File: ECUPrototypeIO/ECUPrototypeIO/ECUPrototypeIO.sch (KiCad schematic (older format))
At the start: 49 parts, among them K1 Relay, K2 Relay, K3 Relay, K4 Relay, K5 Relay, K6 Relay, K7 Relay, K8 Relay, Q1 PN2222A, Q2 PN2222A, Q3 PN2222A, Q4 PN2222A, Q5 PN2222A, SW1 MomentarySwitch, SW2 MomentarySwitch, U1 LM358

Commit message: Sam's Edits (Early January)
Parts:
- removed C3: 470uF, symbol Device:CP1
- removed C4: 1000uF, symbol Device:CP1
- removed D1, D2, D3, D4, D5, D6, D7, D8: D, symbol Device:D
- removed K4, K7: Relay, Relay_THT:Relay_StandexMeder_DIP_LowProfile, symbol Relay:DIPxx-1Cxx-51x
- removed Q1, Q2, Q3, Q4, Q5: PN2222A, Package_TO_SOT_THT:TO-92_Inline, symbol Transistor_BJT:PN2222A
- removed R1, R3, R7, R8: 10K, symbol Device:R
- removed R11, R12, R2: 220, symbol Device:R
- removed SW1: MomentarySwitch, symbol Switch:SW_Push_SPDT
- added C6: 100microF, symbol Device:C
- added J1&2: SafetyLights, symbol Connector:DB9_Female
- added J3: VehicleGeneral, symbol Connector:DB9_Female
- added J4: Steering, symbol Connector:DB9_Female
- added J5: Relay Module, symbol Connector:DB9_Female
- added K? (x2): Relay, Relay_THT:Relay_StandexMeder_DIP_LowProfile, symbol Relay:DIPxx-1Cxx-51x
- added R19: 100, symbol pspice:R
- added R?: 10K, symbol Device:R
- added R? (x2): R, symbol pspice:R
- added SW? (x3): SW_Push_SPDT, symbol Switch:SW_Push_SPDT
- D: renamed from K1; value Relay -> Relay
- renumbered K6 to B, K8 to C
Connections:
- net labels added: 2Pin_Black_POT, 2Pin_Red_POT, 3P_Black_POT, 3Pin_Black_ForRevRelay, 3Pin_Red_ForRevRelay, 3Pin_Red_POT, 3Pin_Yellow_ForRevRelay, 3Pin_Yellow_POT, ACCSafetySignalIN_ltgreen, ACCSignalOUT_Red, ACCSwitch_Black, ACCSwitch_White, Black, Blue, BonusYellow(Estop), EstopIN, GNDREF, Gnd_Black, Gnd_Green, Green, Mode_Red, MotorSpeed, MotorSpeedReading, MotorSpeedReading_White, NotReverse_Blue, Power_White, Red, RelayModuleGnd, RemoteESTOP, Reverse_Red, SafetyLights1, White, Yellow
- net labels removed: +24V, +5V, ESTOP_Out, SafetyLights1_Black, SafetyLights1_Red, SafetyLights1_White, SteeringEncoder_Black, SteeringEncoder_Blue, SteeringEncoder_Green, SteeringEncoder_Red, SteeringPosition
- wire segments 192 -> 178
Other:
- moved on the sheet: B, C, C2, C5, D, K2, K5, R10, R11, R13, R14, R15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

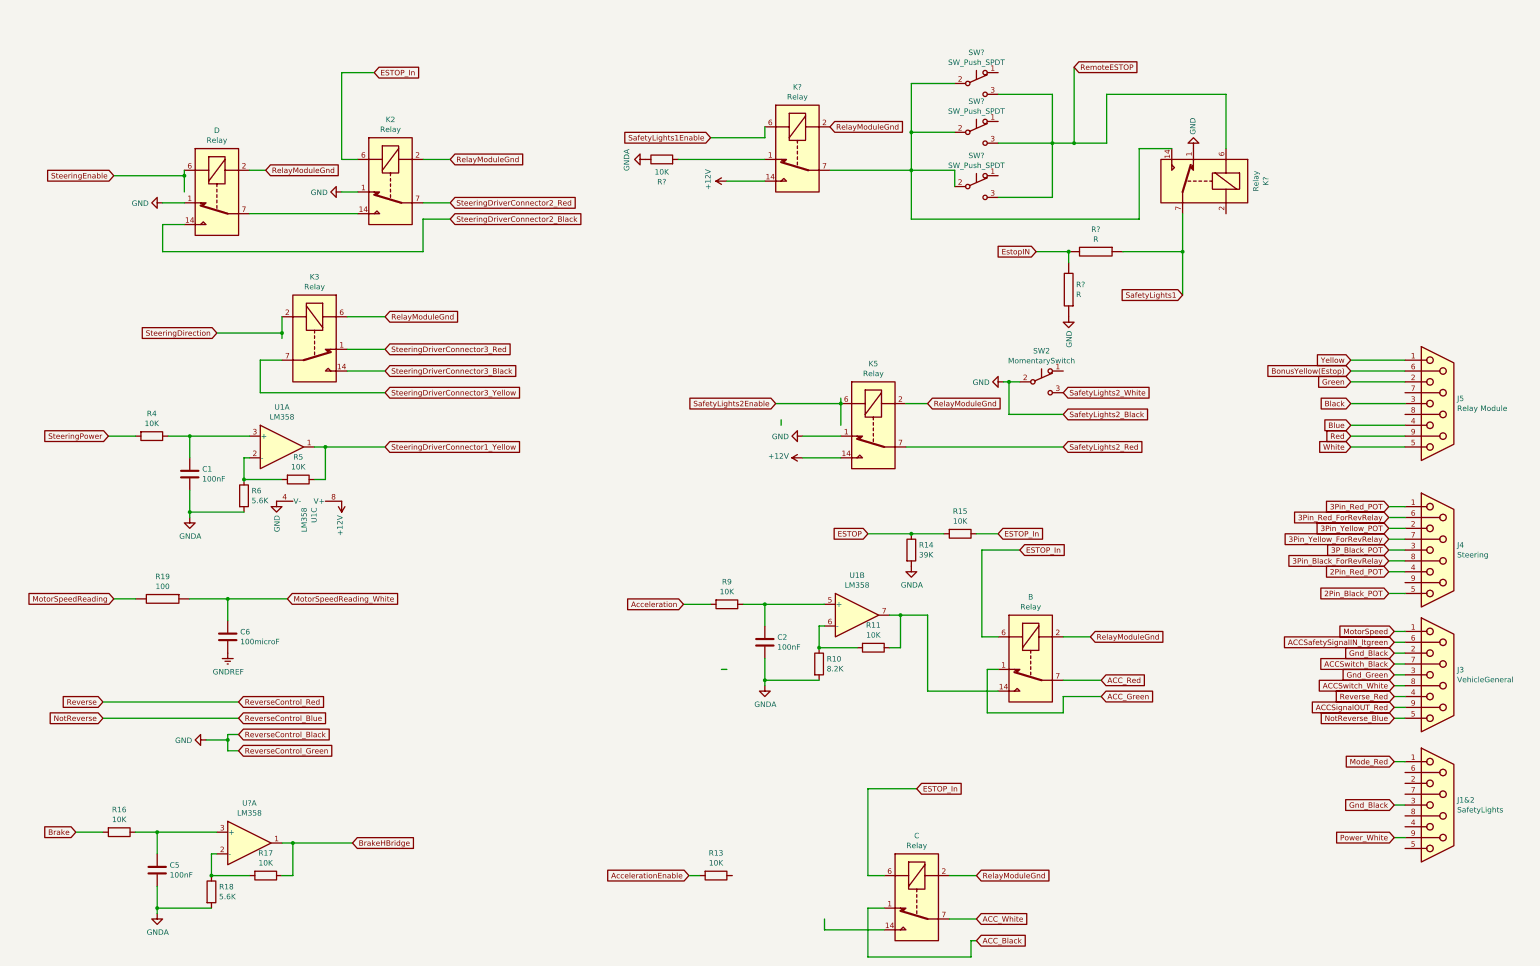
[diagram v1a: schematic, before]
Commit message: ECU Low Level Schematic Edit
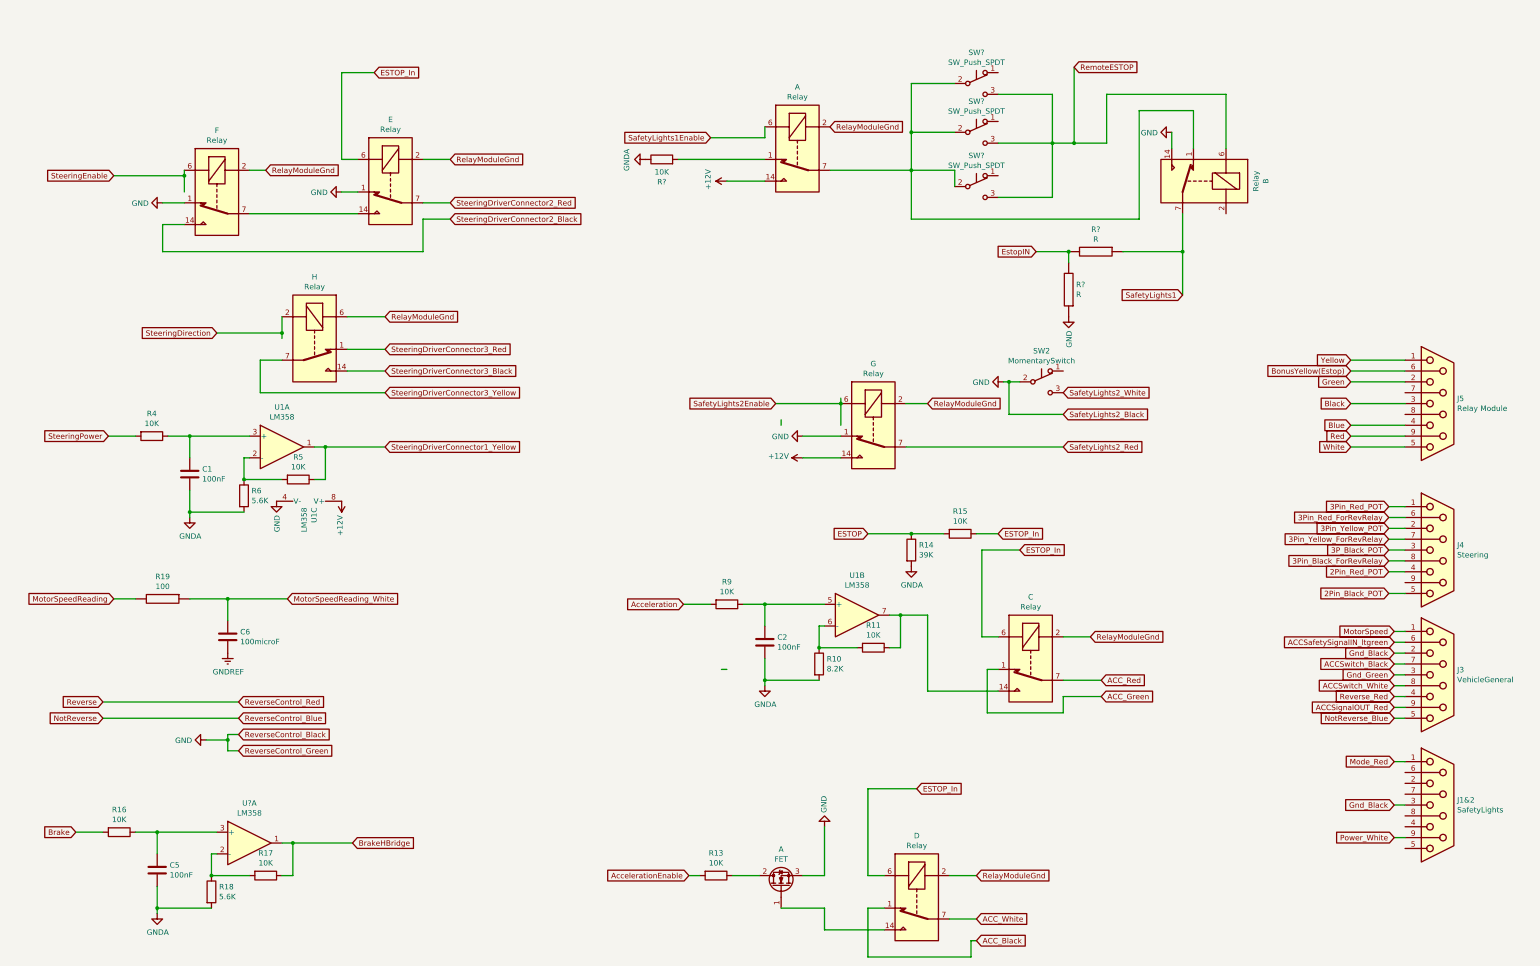
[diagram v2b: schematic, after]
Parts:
- added A: FET, Package_TO_SOT_THT:TO-220-3_Vertical, symbol Transistor_FET:IRF740
- gave numbers to parts that had none: 2
- renumbered B to C, C to D, K2 to E, D to F, K5 to G, K3 to H
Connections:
- wire segments 178 -> 184
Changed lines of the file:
@@
 	3500 1550 3650 1550
 $Comp
-L Relay:DIPxx-1Cxx-51x D
+L Relay:DIPxx-1Cxx-51x F
 U 1 1 5DE030D3
 P 2350 1850
-F 0 "D" V 1783 1850 50  0000 C CNN
+F 0 "F" V 1783 1850 50  0000 C CNN
 F 1 "Relay " V 1874 1850 50  0000 C CNN
 F 2 "Relay_THT:Relay_StandexMeder_DIP_LowProfile" H 2800 1800 50  0001 L CNN
@@
 $EndComp
 $Comp
-L Relay:DIPxx-1Cxx-51x K3
+L Relay:DIPxx-1Cxx-51x H
 U 1 1 5DE4A6EC
 P 3250 3200
-F 0 "K3" V 2683 3200 50  0000 C CNN
+F 0 "H" V 2683 3200 50  0000 C CNN
 F 1 "Relay" V 2774 3200 50  0000 C CNN
 F 2 "Relay_THT:Relay_StandexMeder_DIP_LowProfile" H 3700 3150 50  0001 L CNN
@@
 $EndComp
 $Comp
-L Relay:DIPxx-1Cxx-51x K2
+L Relay:DIPxx-1Cxx-51x E
 U 1 1 5DE2D2DA
 P 3950 1750
-F 0 "K2" V 3383 1750 50  0000 C CNN
+F 0 "E" V 3383 1750 50  0000 C CNN
 F 1 "Relay" V 3474 1750 50  0000 C CNN
 F 2 "Relay_THT:Relay_StandexMeder_DIP_LowProfile" H 4400 1700 50  0001 L CNN
@@
 	8350 8150 8500 8150
 $Comp
-L Relay:DIPxx-1Cxx-51x C
+L Relay:DIPxx-1Cxx-51x D
 U 1 1 5E0CCA91
 P 8800 8350
-F 0 "C" V 8233 8350 50  0000 C CNN
+F 0 "D" V 8233 8350 50  0000 C CNN
 F 1 "Relay" V 8324 8350 50  0000 C CNN
 F 2 "Relay_THT:Relay_StandexMeder_DIP_LowProfile" H 9250 8300 50  0001 L CNN
@@
 	9400 5950 9550 5950
 $Comp
-L Relay:DIPxx-1Cxx-51x B
+L Relay:DIPxx-1Cxx-51x C
 U 1 1 5E11D858
 P 9850 6150
-F 0 "B" V 9283 6150 50  0000 C CNN
+F 0 "C" V 9283 6150 50  0000 C CNN
 F 1 "Relay" V 9374 6150 50  0000 C CNN
 F 2 "Relay_THT:Relay_StandexMeder_DIP_LowProfile" H 10300 6100 50  0001 L CNN
@@
 	8900 6450 9550 6450
 Connection ~ 8650 5750
-Wire Wire Line
-	7950 8550 7950 8650
 Wire Wire Line
 	7950 8650 8500 8650
@@
 $EndComp
 $Comp
-L Relay:DIPxx-1Cxx-51x K?
+L Relay:DIPxx-1Cxx-51x A
 U 1 1 5E271F04
 P 7700 1450
-F 0 "K?" V 7133 1450 50  0000 C CNN
+F 0 "A" V 7133 1450 50  0000 C CNN
 F 1 "Relay" V 7224 1450 50  0000 C CNN
 F 2 "Relay_THT:Relay_StandexMeder_DIP_LowProfile" H 8150 1400 50  0001 L CNN
@@
 	8700 4200 10150 4200
 $Comp
-L Relay:DIPxx-1Cxx-51x K5
+L Relay:DIPxx-1Cxx-51x G
 U 1 1 5DF1B274
 P 8400 4000
-F 0 "K5" V 7833 4000 50  0000 C CNN
+F 0 "G" V 7833 4000 50  0000 C CNN
 F 1 "Relay" V 7924 4000 50  0000 C CNN
 F 2 "Relay_THT:Relay_StandexMeder_DIP_LowProfile" H 8850 3950 50  0001 L CNN
@@
 	13150 5250 13300 5250
 $Comp
-L Relay:DIPxx-1Cxx-51x K?
+L Relay:DIPxx-1Cxx-51x B
 U 1 1 5E9BE291
 P 11450 1750
-F 0 "K?" V 10883 1750 50  0000 C CNN
+F 0 "B" V 10883 1750 50  0000 C CNN
 F 1 "Relay" V 10974 1750 50  0000 C CNN
 F 2 "Relay_THT:Relay_StandexMeder_DIP_LowProfile" H 11900 1700 50  0001 L CNN
@@
 	1    11450 1750
 	-1   0    0    -1
-$EndComp
-Wire Wire Line
-	10850 2100 10850 1450
-Wire Wire Line
-	10850 1450 11150 1450
-$Comp
-L power:GND #PWR?
-U 1 1 5E9E1E08
-P 11350 1450
-F 0 "#PWR?" H 11350 1200 50  0001 C CNN
-F 1 "GND" V 11355 1322 50  0000 R CNN
-F 2 "" H 11350 1450 50  0001 C CNN
-F 3 "" H 11350 1450 50  0001 C CNN
-	1    11350 1450
-	-1   0    0    1
 $EndComp
 Wire Wire Line
@@
 Wire Wire Line
 	12800 4100 13300 4100
+Wire Wire Line
+	10850 1100 11350 1100
+Wire Wire Line
+	10850 1100 10850 2100
+Wire Wire Line
+	11350 1100 11350 1450
+$Comp
+L power:GND #PWR?
+U 1 1 5E2E167D
+P 11150 1300
+F 0 "#PWR?" H 11150 1050 50  0001 C CNN
+F 1 "GND" V 11155 1172 50  0000 R CNN
+F 2 "" H 11150 1300 50  0001 C CNN
+F 3 "" H 11150 1300 50  0001 C CNN
+	1    11150 1300
+	0    1    1    0
+$EndComp
+Wire Wire Line
+	11150 1450 11150 1300
+$Comp
+L Transistor_FET:IRF740 A
+U 1 1 5E2EE751
+P 7550 8250
+F 0 "A" V 7892 8250 50  0000 C CNN
+F 1 "FET" V 7801 8250 50  0000 C CNN
+F 2 "Package_TO_SOT_THT:TO-220-3_Vertical" H 7800 8175 50  0001 L CIN
+F 3 "http://www.vishay.com/docs/91054/91054.pdf" H 7550 8250 50  0001 L CNN
+	1    7550 8250
+	0    -1   -1   0
+$EndComp
+Wire Wire Line
+	7550 8450 7950 8450
+Wire Wire Line
+	7950 8450 7950 8650
+Wire Wire Line
+	7100 8150 7350 8150
+Wire Wire Line
+	7750 8150 7950 8150
+Wire Wire Line
+	7950 8150 7950 7700
+$Comp
+L power:GND #PWR?
+U 1 1 5E321D34
+P 7950 7700
+F 0 "#PWR?" H 7950 7450 50  0001 C CNN
+F 1 "GND" V 7955 7572 50  0000 R CNN
+F 2 "" H 7950 7700 50  0001 C CNN
+F 3 "" H 7950 7700 50  0001 C CNN
+	1    7950 7700
+	-1   0    0    1
+$EndComp
 $EndSCHEMATC
